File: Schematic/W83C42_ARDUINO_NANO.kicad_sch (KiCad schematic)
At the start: 23 parts, among them J2 Mini-DIN-6, J3 DIN-5, U1 74HC14, Y1 Crystal

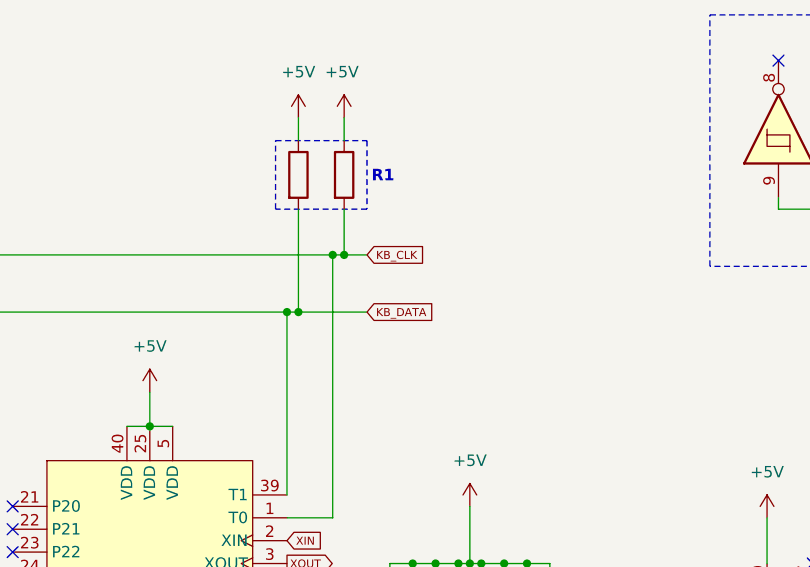
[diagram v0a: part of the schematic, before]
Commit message: Fixed the labels on the schematic, the KB_CLK and KB_DATA labels were switched up
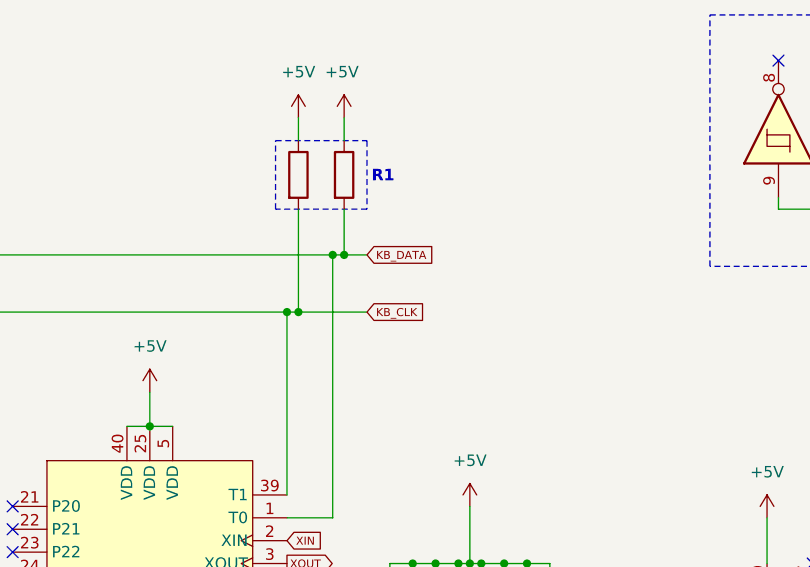
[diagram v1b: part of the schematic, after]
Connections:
- net KB_CLK: now also R11.2, U1.6, W83C42.39 (T1); no longer R10.2, U1.4, W83C42.1 (T0)
- net KB_DATA: now also R10.2, U1.4, W83C42.1 (T0); no longer R11.2, U1.6, W83C42.39 (T1)
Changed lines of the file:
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@@
+		)
+	)
+	(global_label "KB_DATA"
+		(shape input)
+		(at 170.18 49.53 0)
+		(fields_autoplaced yes)
+		(effects
+			(font
+				(size 0.889 0.889)
+				(thickness 0.1111)
+			)
+			(justify left)
+		)
+		(property "Intersheetrefs" "${INTERSHEET_REFS}"
+			(at 177.8151 49.53 0)
+			(effects
+				(font
+					(size 1.27 1.27)
+				)
+				(justify left)
+				(hide yes)
+			)
 		)
 	)
@@
 		)
 	)
+	(global_label "KB_CLK"
+		(shape input)
+		(at 170.18 55.88 0)
+		(fields_autoplaced yes)
+		(effects
+			(font
+				(size 0.889 0.889)
+				(thickness 0.1111)
+			)
+			(justify left)
+		)
+		(property "Intersheetrefs" "${INTERSHEET_REFS}"
+			(at 177.2225 55.88 0)
+			(effects
+				(font
+					(size 1.27 1.27)
+				)
+				(justify left)
+				(hide yes)
+			)
+		)
+	)
 	(global_label "GND"
 		(shape input)
@@
 		)
 	)
+	(global_label "#WR"
+		(shape input)
+		(at 161.29 96.52 0)
+		(fields_autoplaced yes)
+		(effects
+			(font
+				(size 0.889 0.889)
+				(thickness 0.0953)
+			)
+			(justify left)
+		)
+		(property "Intersheetrefs" "${INTERSHEET_REFS}"
+			(at 166.0945 96.52 0)
+			(effects
+				(font
+					(size 1.27 1.27)
+				)
+				(justify left)
+				(hide yes)
+			)
+		)
+	)
+	(global_label "XOUT"
+		(shape input)
+		(at 53.34 71.12 0)
+		(fields_autoplaced yes)
+		(effects
+			(font
+				(size 0.889 0.889)
+				(thickness 0.1111)
+			)
+			(justify left)
+		)
+		(property "Intersheetrefs" "${INTERSHEET_REFS}"
+			(at 58.8161 71.12 0)
+			(effects
+				(font
+					(size 1.27 1.27)
+				)
+				(justify left)
+				(hide yes)
+			)
+		)
+	)
+	(global_label "#CS"
+		(shape output)
+		(at 229.87 109.22 0)
+		(fields_autoplaced yes)
+		(effects
+			(font
+				(size 0.889 0.889)
+				(thickness 0.0953)
+			)
+			(justify left)
+		)
+		(property "Intersheetrefs" "${INTERSHEET_REFS}"
+			(at 234.5052 109.22 0)
+			(effects
+				(font
+					(size 1.27 1.27)
+				)
+				(justify left)
+				(hide yes)
+			)
+		)
+	)
+	(global_label "#RST"
+		(shape input)
+		(at 130.81 100.33 180)
+		(fields_autoplaced yes)
+		(effects
+			(font
+				(size 0.889 0.889)
+				(thickness 0.0953)
+			)
+			(justify right)
+		)
+		(property "Intersheetrefs" "${INTERSHEET_REFS}"
+			(at 125.4975 100.33 0)
+			(effects
+				(font
+					(size 1.27 1.27)
+				)
+				(justify right)
+				(hide yes)
+			)
+		)
+	)
+	(global_label "#WR"
+		(shape output)
+		(at 204.47 127 180)
+		(fields_autoplaced yes)
+		(effects
+			(font
+				(size 0.889 0.889)
+				(thickness 0.0953)
+			)
+			(justify right)
+		)
+		(property "Intersheetrefs" "${INTERSHEET_REFS}"
+			(at 199.6655 127 0)
+			(effects
+				(font
+					(size 1.27 1.27)
+				)
+				(justify right)
+				(hide yes)
+			)
+		)
+	)
+	(global_label "XIN"
+		(shape output)
+		(at 54.61 96.52 0)
+		(fields_autoplaced yes)
+		(effects
+			(font
+				(size 0.889 0.889)
+				(thickness 0.1111)
+			)
+			(justify left)
+		)
+		(property "Intersheetrefs" "${INTERSHEET_REFS}"
+			(at 58.9008 96.52 0)
+			(effects
+				(font
+					(size 1.27 1.27)
+				)
+				(justify left)
+				(hide yes)
+			)
+		)
+	)
 	(global_label "KB_DATA"
-		(shape input)
-		(at 170.18 55.88 0)
-		(fields_autoplaced yes)
-		(effects
-			(font
-				(size 0.889 0.889)
-				(thickness 0.1111)
-			)
-			(justify left)
-		)
-		(property "Intersheetrefs" "${INTERSHEET_REFS}"
-			(at 177.8151 55.88 0)
-			(effects
-				(font
-					(size 1.27 1.27)
-				)
-				(justify left)
-				(hide yes)
-			)
-		)
-	)
-	(global_label "#WR"
-		(shape input)
-		(at 161.29 96.52 0)
-		(fields_autoplaced yes)
-		(effects
-			(font
-				(size 0.889 0.889)
-				(thickness 0.0953)
-			)
-			(justify left)
-		)
-		(property "Intersheetrefs" "${INTERSHEET_REFS}"
-			(at 166.0945 96.52 0)
-			(effects
-				(font
-					(size 1.27 1.27)
-				)
-				(justify left)
-				(hide yes)
-			)
-		)
-	)
-	(global_label "XOUT"
-		(shape input)
-		(at 53.34 71.12 0)
-		(fields_autoplaced yes)
-		(effects
-			(font
-				(size 0.889 0.889)
-				(thickness 0.1111)
-			)
-			(justify left)
-		)
-		(property "Intersheetrefs" "${INTERSHEET_REFS}"
-			(at 58.8161 71.12 0)
-			(effects
-				(font
-					(size 1.27 1.27)
-				)
-				(justify left)
-				(hide yes)
-			)
-		)
-	)
-	(global_label "#CS"
-		(shape output)
-		(at 229.87 109.22 0)
-		(fields_autoplaced yes)
-		(effects
-			(font
-				(size 0.889 0.889)
-				(thickness 0.0953)
-			)
-			(justify left)
-		)
-		(property "Intersheetrefs" "${INTERSHEET_REFS}"
-			(at 234.5052 109.22 0)
-			(effects
-				(font
-					(size 1.27 1.27)
-				)
-				(justify left)
-				(hide yes)
-			)
-		)
-	)
-	(global_label "#RST"
-		(shape input)
-		(at 130.81 100.33 180)
-		(fields_autoplaced yes)
-		(effects
-			(font
-				(size 0.889 0.889)
-				(thickness 0.0953)
-			)
-			(justify right)
-		)
-		(property "Intersheetrefs" "${INTERSHEET_REFS}"
-			(at 125.4975 100.33 0)
-			(effects
-				(font
-					(size 1.27 1.27)
-				)
-				(justify right)
-				(hide yes)
-			)
-		)
-	)
-	(global_label "#WR"
-		(shape output)
-		(at 204.47 127 180)
-		(fields_autoplaced yes)
-		(effects
-			(font
-				(size 0.889 0.889)
-				(thickness 0.0953)
-			)
-			(justify right)
-		)
-		(property "Intersheetrefs" "${INTERSHEET_REFS}"
-			(at 199.6655 127 0)
-			(effects
-				(font
-					(size 1.27 1.27)
-				)
-				(justify right)
-				(hide yes)
-			)
-		)
-	)
-	(global_label "XIN"
-		(shape output)
-		(at 54.61 96.52 0)
-		(fields_autoplaced yes)
-		(effects
-			(font
-				(size 0.889 0.889)
-				(thickness 0.1111)
-			)
-			(justify left)
-		)
-		(property "Intersheetrefs" "${INTERSHEET_REFS}"
-			(at 58.9008 96.52 0)
-			(effects
-				(font
-					(size 1.27 1.27)
-				)
-				(justify left)
-				(hide yes)
-			)
-		)
-	)
-	(global_label "KB_DATA"
 		(shape output)
 		(at 43.18 127 0)
@@
 				(hide yes)
 			)
-		)
-	)
-	(global_label "KB_CLK"
-		(shape input)
-		(at 170.18 49.53 0)
-		(fields_autoplaced yes)
-		(effects
-			(font
-				(size 0.889 0.889)
-				(thickness 0.1111)
-			)
-			(justify left)
-		)
-		(property "Intersheetrefs" "${INTERSHEET_REFS}"
-			(at 177.2225 49.53 0)
-			(effects
-				(font
-					(size 1.27 1.27)
-				)
-				(justify left)
-				(hide yes)
-			)
